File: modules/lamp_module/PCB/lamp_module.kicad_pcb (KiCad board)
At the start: 2 copper layers, 61 x 64 mm, 40 parts, among them J1 Screw_Terminal_01x02, J2 Screw_Terminal_01x02, J3 Conn_01x06_Socket, K1 12V 5A, K2 12V 5A, Q1 2N7002H, Q2 2N7002H, U1 AMS1117-3.3, U2 ESP-12E, U4 PC817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

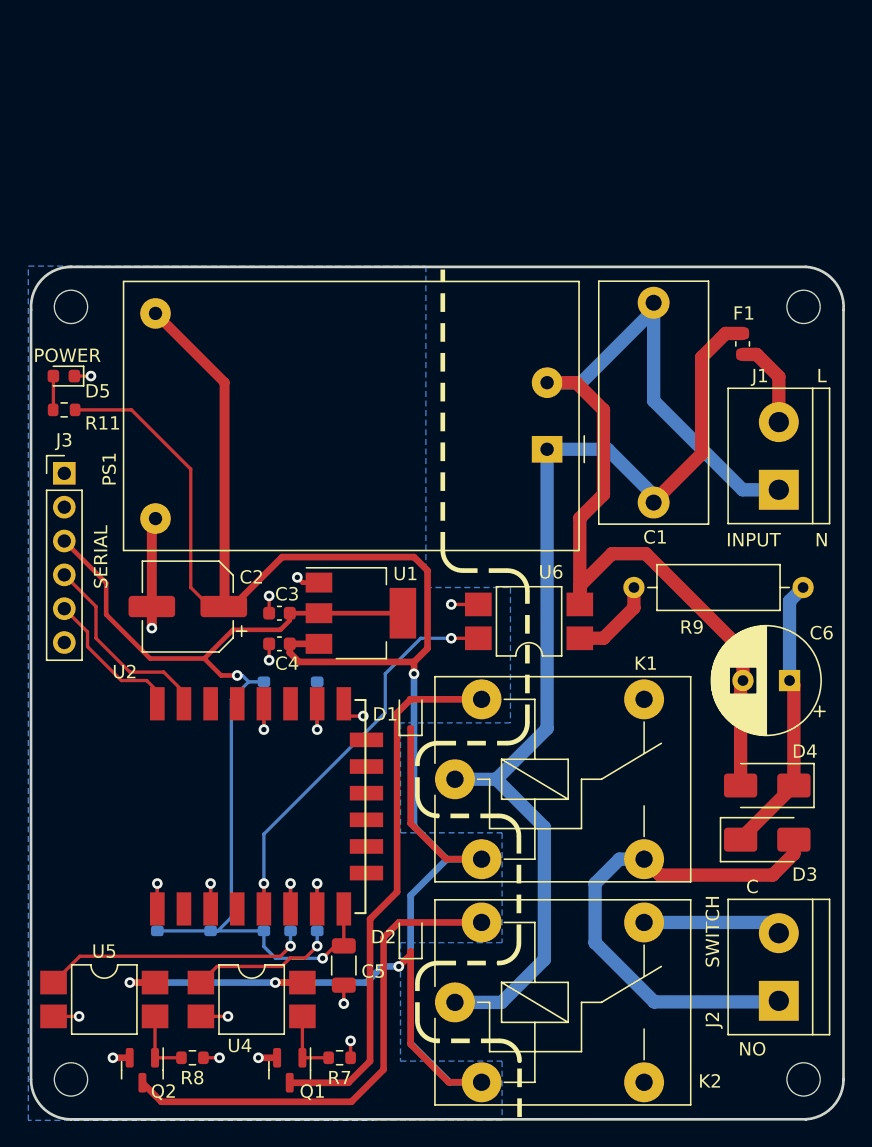
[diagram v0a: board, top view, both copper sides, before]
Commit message: PCB simplified and improved
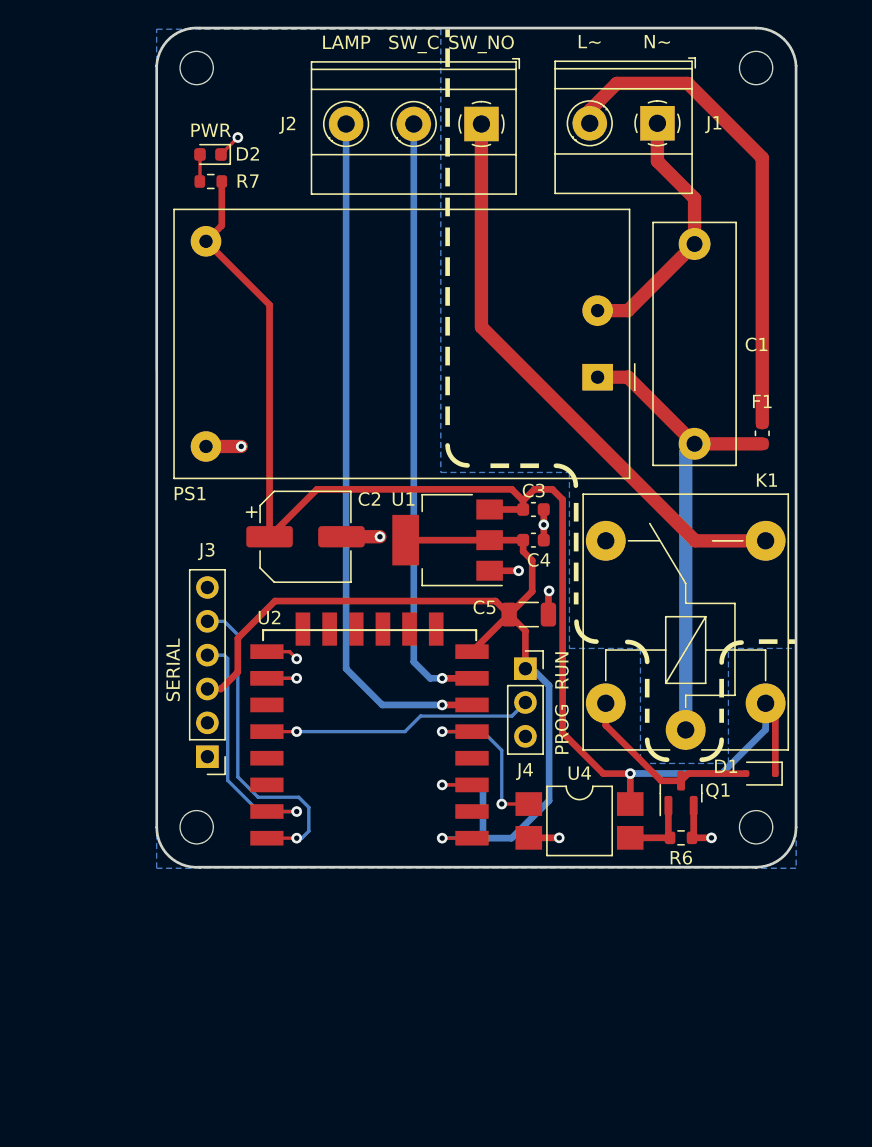
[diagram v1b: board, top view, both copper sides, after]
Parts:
- removed C6: 1uF, Capacitor_THT:CP_Radial_D8.0mm_P3.50mm
- removed D3, D4: 1N4007, Diode_SMD:D_SMA
- removed D5: LED, LED_SMD:LED_0603_1608Metric
- removed K2: 12V 5A, Relay_THT:Relay_SPDT_Finder_36.11
- removed Q2: 2N7002H, Package_TO_SOT_SMD:SOT-23
- removed R10, R3, R8: 10k, Resistor_SMD:R_0603_1608Metric
- removed R11: 2.2k, Resistor_SMD:R_0603_1608Metric
- removed R9: 56k, Resistor_THT:R_Axial_DIN0309_L9.0mm_D3.2mm_P12.70mm_Horizontal
- removed U5, U6: PC817, Package_DIP:SMDIP-4_W7.62mm
- added G***: LOGO, LOGO, B.Cu at (155.0, 74.6)
- added J4: Conn_01x03_Socket, Connector_PinSocket_2.54mm:PinSocket_1x03_P2.54mm_Vertical, F.Cu at (156.2, 99.0)
- C1: footprint Capacitor_THT:C_Rect_L18.0mm_W8.0mm_P15.00mm_FKS3_FKP3 -> Capacitor_THT:C_Rect_L18.0mm_W6.0mm_P15.00mm_FKS3_FKP3
- D2: value 1N4148 -> LED; footprint Diode_SMD:D_SOD-323F -> LED_SMD:LED_0603_1608Metric
- J1: footprint TerminalBlock:TerminalBlock_bornier-2_P5.08mm -> TerminalBlock_Phoenix:TerminalBlock_Phoenix_MKDS-1,5-2-5.08_1x02_P5.08mm_Horizontal
- J2: value Screw_Terminal_01x02 -> Screw_Terminal_01x03; footprint TerminalBlock:TerminalBlock_bornier-2_P5.08mm -> TerminalBlock_Phoenix:TerminalBlock_Phoenix_MKDS-1,5-3-5.08_1x03_P5.08mm_Horizontal
- R6: value 390 -> 10k; moved to F.Cu
- R7: value 10k -> 2.2k
- moved REF** 76.0 mm to (173.6, 53.9), turned to -90 degrees
- moved J2 69.5 mm to (152.9, 58.1), turned to 180 degrees
- moved R7 66.5 mm to (132.6, 62.4)
- moved D2 60.6 mm to (132.6, 60.4), turned to 180 degrees
- moved REF** 54.8 mm to (173.6, 110.9), turned to -90 degrees
- moved REF** 49.0 mm to (131.6, 53.9), turned to 90 degrees
- moved REF** 40.2 mm to (131.6, 110.9), turned to 90 degrees
- moved Q1 36.0 mm to (167.9, 108.4), turned to 90 degrees
- moved R6 30.0 mm to (167.9, 111.7), turned to 0 degrees
- moved C5 29.8 mm to (156.5, 95.0), turned to 0 degrees
- moved J1 29.0 mm to (166.1, 58.1), turned to 180 degrees
- moved U4 28.0 mm to (160.3, 110.4)
- moved D1 26.7 mm to (173.9, 106.9), turned to 180 degrees
- moved R2 24.4 mm to (152.2, 111.7), turned to 180 degrees
- moved J3 23.8 mm to (132.4, 105.6), turned to 180 degrees
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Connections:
- D2 pad 1: +12V -> GND
- J2 pad 1: SWITCH_NO -> LAMP
- J2 pad 2: Net-(J2-Pin_2) -> SWITCH_NO
- K1 pad 14: SWITCH_NO -> LAMP
- R5 pad 2: RELAY_P -> RELAY
- R6 pad 1: Net-(R6-Pad1) -> Net-(Q1-G)
- R6 pad 2: RELAY_S -> GND
- R7 pad 1: Net-(Q1-G) -> Net-(D2-A)
- R7 pad 2: GND -> +12V
- U2 pad 12: Net-(U2-GPIO0) -> FLASH
- U2 pad 5: FEEDBACK -> RELAY
- U2 pad 6: RELAY_S -> SWITCH_C
- U2 pad 7: RELAY_P -> SWITCH_NO
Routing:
- net +12V: track 176.7 -> 103.6 mm, vias 4 -> 1
- net NEUT: track 78.6 -> 19.6 mm
- net SWITCH_C: track 0.00 -> 50.8 mm, vias 0 -> 1
- net LAMP: track 0.00 -> 42.9 mm
- net LINE: track 78.7 -> 36.2 mm
- net Net-(D2-A): track 37.4 -> 2.04 mm
- net FEEDBACK: track 30.8 -> 0.00 mm, vias 2 -> 0
- net Net-(J1-Pin_2): track 6.82 -> 37.0 mm
- net Net-(D1-A): track 40.5 -> 14.1 mm
- net Net-(D3-K): track 21.1 -> 0.00 mm
- net Net-(R6-Pad1): track 20.1 -> 0.00 mm, vias 1 -> 0
- net FLASH: track 0.00 -> 19.6 mm, vias 0 -> 1
- net RX: track 11.8 -> 24.1 mm, vias 0 -> 1
- net Net-(J2-Pin_2): track 10.5 -> 0.00 mm
- net SWITCH_NO: track 38.0 -> 44.6 mm, vias 0 -> 1
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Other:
- board size 61 x 64 mm -> 48 x 63 mm
- board text added: "HAP - Lamp Module X1 V1.1"
- board text removed: "C"
- board text removed: "L"
- board text removed: "Lamp Module X1 V1.0"
- board text removed: "N"
- board text removed: "NO"
